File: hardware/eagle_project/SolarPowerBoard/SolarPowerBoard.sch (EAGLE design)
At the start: 82 parts, among them IC1 BQ29700DSET_BQ29700DSET, IC3 TPS63031DSKT_TPS63031DSKT, J2 105017-0001_105017-0001, J5 XG8S-0331_XG8S-0331, K1 G6E-134P-US_DC5_G6E-134P-US_D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, Q3 DAVIDE_FDN302P, U4 MCP73831T-2ACI_OT_MCP73831T-2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

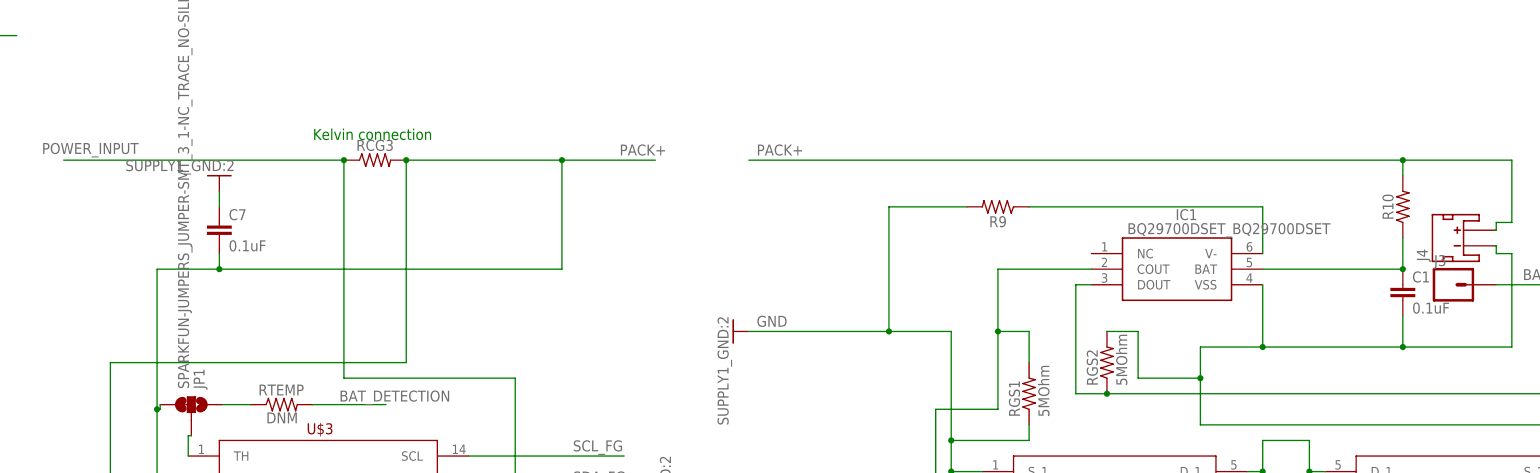
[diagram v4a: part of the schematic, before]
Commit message: Changed sense resistor
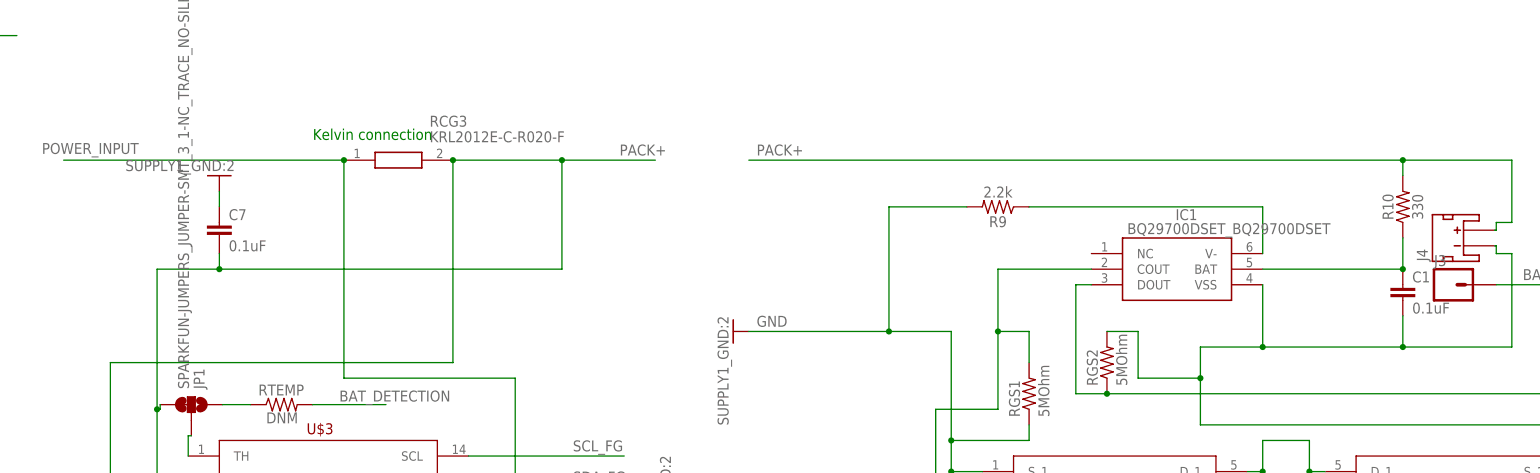
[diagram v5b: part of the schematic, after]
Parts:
- R10: value (none) -> 330
- R9: value (none) -> 2.2k
- RCG3: value (none) -> KRL2012E-C-R020-F; device SolarPowerBoard:SPARKFUN-RESISTORS_RESISTOR0805:1 -> SolarPowerBoard:KRL2012E-C-R020-F; OC_NEWARK unknown -> (none)
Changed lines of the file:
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@@
 <attribute name="OC_NEWARK" value="78X4150"/>
 </part>
-<part name="R9" library="SolarPowerBoard" deviceset="SPARKFUN-RESISTORS_RESISTOR*?:1" device="0805" value=" ">
+<part name="R9" library="SolarPowerBoard" deviceset="SPARKFUN-RESISTORS_RESISTOR*?:1" device="0805" value="2.2k">
 <attribute name="MF" value=""/>
 <attribute name="MPN" value="CR0805-FX-2201ELF"/>
 <attribute name="OC_NEWARK" value="06X5164"/>
 </part>
-<part name="R10" library="SolarPowerBoard" deviceset="SPARKFUN-RESISTORS_RESISTOR*?:1" device="0805" value=" ">
+<part name="R10" library="SolarPowerBoard" deviceset="SPARKFUN-RESISTORS_RESISTOR*?:1" device="0805" value="330">
 <attribute name="MF" value=""/>
 <attribute name="MPN" value="ERJ-6GEYJ331V"/>
@@
 </part>
 <part name="GND21" library="SolarPowerBoard" deviceset="SUPPLY1_GND*?:2" device=""/>
-<part name="RCG3" library="SolarPowerBoard" deviceset="SPARKFUN-RESISTORS_RESISTOR*?:1" device="0805" value=" ">
-<attribute name="MF" value=""/>
-<attribute name="MPN" value=""/>
-<attribute name="OC_NEWARK" value="unknown"/>
-</part>
 <part name="U$3" library="SolarPowerBoard" deviceset="SOLARCOMPONENTS_MAX17260" device="">
 <attribute name="MF" value=""/>
@@
 </part>
 <part name="L1" library="inductors" library_urn="urn:adsk.eagle:library:243" deviceset="EMC9714" device="" package3d_urn="urn:adsk.eagle:package:15060/1"/>
+<part name="RCG3" library="SolarPowerBoard" deviceset="KRL2012E-C-R020-F" device=""/>
 </parts>
 <sheets>
@@
 </instance>
 <instance part="GND21" gate="1" x="360.68" y="33.02" rot="R270"/>
-<instance part="RCG3" gate="G$1" x="302.26" y="60.96">
-<attribute name="NAME" x="302.26" y="62.484" size="1.778" layer="95" font="vector" align="bottom-center"/>
-<attribute name="VALUE" x="302.26" y="59.436" size="1.778" layer="96" font="vector" align="top-center"/>
-<attribute name="OC_NEWARK" x="302.26" y="60.96" size="1.778" layer="96" display="off"/>
-<attribute name="MF" x="302.26" y="60.96" size="1.778" layer="96" display="off"/>
-<attribute name="MPN" x="302.26" y="60.96" size="1.778" layer="96" display="off"/>
-</instance>
 <instance part="U$3" gate="G$1" x="294.64" y="5.08">
 <attribute name="NAME" x="291.084" y="16.256" size="1.778" layer="94"/>
@@
 <attribute name="NAME" x="24.13" y="75.946" size="1.778" layer="95"/>
 <attribute name="VALUE" x="24.003" y="70.612" size="1.778" layer="96"/>
+</instance>
+<instance part="RCG3" gate="G$1" x="297.18" y="60.96">
+<attribute name="NAME" x="311.15" y="67.31" size="1.778" layer="95" align="center-left"/>
+<attribute name="VALUE" x="311.15" y="64.77" size="1.778" layer="96" align="center-left"/>
 </instance>
 </instances>
@@
 <segment>
 <pinref part="U$3" gate="G$1" pin="CSN"/>
-<wire x1="307.34" y1="27.94" x2="259.08" y2="27.94" width="0.1524" layer="91"/>
+<wire x1="314.96" y1="27.94" x2="259.08" y2="27.94" width="0.1524" layer="91"/>
 <wire x1="259.08" y1="27.94" x2="259.08" y2="-17.78" width="0.1524" layer="91"/>
 <wire x1="259.08" y1="-17.78" x2="271.78" y2="-17.78" width="0.1524" layer="91"/>
@@
 <wire x1="266.7" y1="20.32" x2="266.7" y2="43.18" width="0.1524" layer="91"/>
 <wire x1="266.7" y1="43.18" x2="276.86" y2="43.18" width="0.1524" layer="91"/>
-<pinref part="RCG3" gate="G$1" pin="2"/>
 <wire x1="276.86" y1="43.18" x2="332.74" y2="43.18" width="0.1524" layer="91"/>
-<wire x1="332.74" y1="60.96" x2="307.34" y2="60.96" width="0.1524" layer="91"/>
+<wire x1="332.74" y1="60.96" x2="314.96" y2="60.96" width="0.1524" layer="91"/>
 <wire x1="332.74" y1="43.18" x2="332.74" y2="60.96" width="0.1524" layer="91"/>
 <wire x1="276.86" y1="43.18" x2="276.86" y2="45.72" width="0.1524" layer="91"/>
 <junction x="276.86" y="43.18"/>
 <pinref part="C7" gate="G$1" pin="2"/>
-<wire x1="307.34" y1="27.94" x2="307.34" y2="60.96" width="0.1524" layer="91"/>
-<junction x="307.34" y="60.96"/>
+<wire x1="314.96" y1="27.94" x2="314.96" y2="60.96" width="0.1524" layer="91"/>
 <pinref part="JP1" gate="G$1" pin="3"/>
 <wire x1="267.208" y1="21.082" x2="267.208" y2="20.32" width="0.1524" layer="91"/>
@@
 <junction x="332.74" y="60.96"/>
 <label x="342.138" y="61.722" size="1.778" layer="95"/>
+<pinref part="RCG3" gate="G$1" pin="2"/>
+<junction x="314.96" y="60.96"/>
 </segment>
 </net>
@@
 <pinref part="U$3" gate="G$1" pin="CSPH"/>
 <wire x1="317.5" y1="-7.62" x2="325.12" y2="-7.62" width="0.1524" layer="91"/>
-<pinref part="RCG3" gate="G$1" pin="1"/>
 <wire x1="297.18" y1="25.4" x2="297.18" y2="60.96" width="0.1524" layer="91"/>
 <wire x1="251.46" y1="60.96" x2="297.18" y2="60.96" width="0.1524" layer="91"/>
+<label x="247.904" y="61.976" size="1.778" layer="95"/>
+<pinref part="RCG3" gate="G$1" pin="1"/>
 <junction x="297.18" y="60.96"/>
-<label x="247.904" y="61.976" size="1.778" layer="95"/>
-</segment>
-<segment>
+</segment>
+<segment>

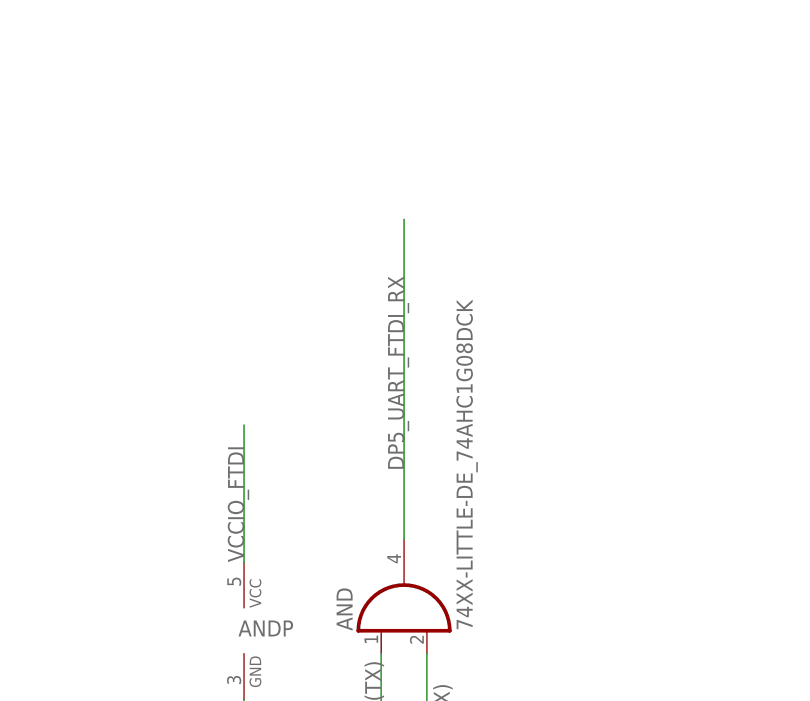
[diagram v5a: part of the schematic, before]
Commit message: Added 0ohm resistor between UART AND port and RX pin. Removed library autosave files.
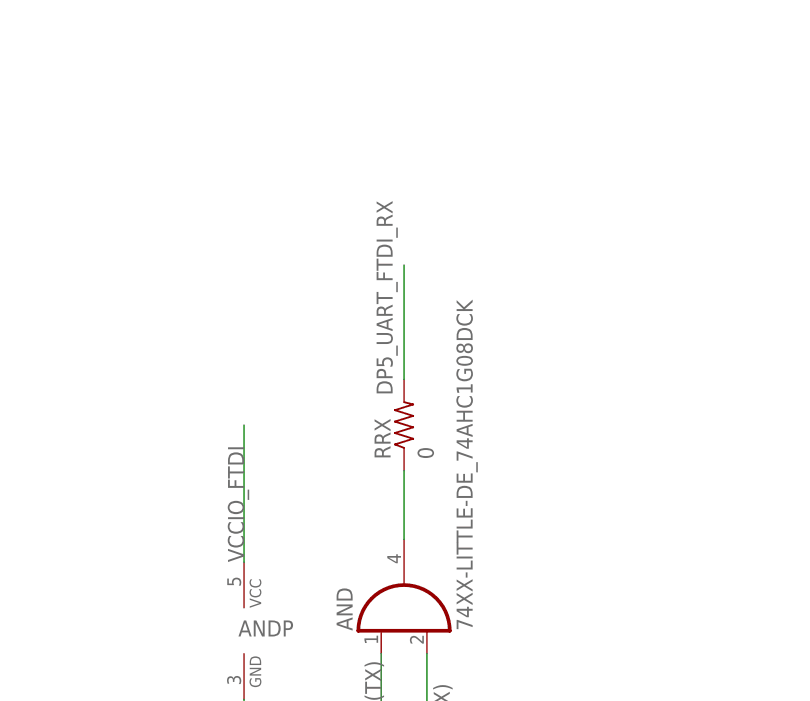
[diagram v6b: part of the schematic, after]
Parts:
- added RRX: 0, resistor:R-US_R0805
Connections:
- net DP5_UART_FTDI_RX: now also RRX.1, RRX.2
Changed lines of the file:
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@@
 <part name="L1" library="inductors" library_urn="urn:adsk.eagle:library:243" deviceset="EMC9714" device="" package3d_urn="urn:adsk.eagle:package:15060/1"/>
 <part name="RCG3" library="SolarPowerBoard" deviceset="KRL2012E-C-R020-F" device=""/>
+<part name="RRX" library="resistor" library_urn="urn:adsk.eagle:library:348" deviceset="R-US_" device="R0805" package3d_urn="urn:adsk.eagle:package:23553/2" value="0"/>
 </parts>
 <sheets>
@@
 <attribute name="NAME" x="311.15" y="67.31" size="1.778" layer="95" align="center-left"/>
 <attribute name="VALUE" x="311.15" y="64.77" size="1.778" layer="96" align="center-left"/>
+</instance>
+<instance part="RRX" gate="G$1" x="-83.82" y="104.14" rot="R90">
+<attribute name="NAME" x="-85.3186" y="100.33" size="1.778" layer="95" rot="R90"/>
+<attribute name="VALUE" x="-80.518" y="100.33" size="1.778" layer="96" rot="R90"/>
 </instance>
 </instances>
@@
 <net name="DP5_UART_FTDI_RX" class="0">
 <segment>
-<pinref part="AND" gate="A" pin="O"/>
-<wire x1="-83.82" y1="91.44" x2="-83.82" y2="127" width="0.1524" layer="91"/>
-<label x="-83.82" y="99.06" size="1.778" layer="95" rot="R90"/>
-</segment>
-<segment>
 <pinref part="FT230XQ-R" gate="G$1" pin="RXD"/>
 <pinref part="RX_TX" gate="G$1" pin="2"/>
@@
 <label x="102.616" y="156.718" size="1.778" layer="95"/>
 </segment>
+<segment>
+<pinref part="AND" gate="A" pin="O"/>
+<wire x1="-83.82" y1="91.44" x2="-83.82" y2="99.06" width="0.1524" layer="91"/>
+<pinref part="RRX" gate="G$1" pin="1"/>
+</segment>
+<segment>
+<pinref part="RRX" gate="G$1" pin="2"/>
+<wire x1="-83.82" y1="109.22" x2="-83.82" y2="121.92" width="0.1524" layer="91"/>
+<label x="-85.09" y="107.442" size="1.778" layer="95" rot="R90"/>
+</segment>
 </net>

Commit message: commiting the PCB printed ad eurocircuit (very first version)
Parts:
- removed C1-1, C1-2: 4.7uF, SolarPowerBoard:SPARKFUN-CAPACITORS_4.7UF0603
- removed D5: RED, SolarPowerBoard:SPARKFUN-LED_LED0603
- removed IC1: BQ29700DSET_BQ29700DSET, SolarPowerBoard:BQ29700DSET_BQ29700DSET
- removed RCG3: KRL2012E-C-R020-F, SolarPowerBoard:KRL2012E-C-R020-F
- removed RX: ORANGE, SparkFun-LED:LED0603
- removed TX: YELLOW, SparkFun-LED:LED0603
- added C13: 10u, SolarPowerBoard:SPARKFUN-CAPACITORS_10UF-0805-10V-10%
- added LED_CH, LED_RX, LED_TX: (no value), SolarPowerBoard:LED0603
- added R5: 0.02, SolarPowerBoard:FCSL90R020DER
- added U6: MCP73831T-2ACI_OT_MCP73831T-2ACI/OT, SolarPowerBoard:MCP73831T-2ACI_OT_MCP73831T-2ACI/OT
- C1, C7, CMPP: value 0.1uF -> 100n; device SolarPowerBoard:SPARKFUN-CAPACITORS_0.1UF-0603-100V-10% -> SolarPowerBoard:SPARKFUN-CAPACITORS_10UF-0805-10V-10%; MF (none) -> AVX CORPORATION; MPN MC0603B104K160CT -> TPSP106M010R2000; OC_NEWARK 06R4923 -> 22K2788
- C10: value 470nF -> 470n; device SolarPowerBoard:RESISTOR_C-EUC0805 -> SolarPowerBoard:SPARKFUN-CAPACITORS_10UF-0805-10V-10%; MF (none) -> AVX CORPORATION; MPN C0805C474K8RACTU -> TPSP106M010R2000; OC_NEWARK 07X0956 -> 22K2788
- C11, C12: device SolarPowerBoard:SPARKFUN-CAPACITORS_CAP0603-CAP -> SolarPowerBoard:SPARKFUN-CAPACITORS_10UF-0805-10V-10%; MF (none) -> AVX CORPORATION; MPN (none) -> TPSP106M010R2000; OC_NEWARK (none) -> 22K2788
- C14: value 10nF -> 10n
- C15, C16: value 47pF -> 47p
- C2, C3, C4: value 10uF -> 10u
- C24, C26, C8, C9: value 100nF -> 100n
- C25: value 4.7uF -> 4.7u
- C5: value 0.1uF -> 100n; device SolarPowerBoard:SPARKFUN-CAPACITORS_0.1UF-0603-25V-5% -> SolarPowerBoard:SPARKFUN-CAPACITORS_10UF-0805-10V-10%; MF (none) -> AVX CORPORATION; MPN MC0603B104K160CT -> TPSP106M010R2000; OC_NEWARK 06R4923 -> 22K2788
- C6: value 470pF -> 470p; device SolarPowerBoard:SPARKFUN-CAPACITORS_470PF-0603-50V-5% -> SolarPowerBoard:SPARKFUN-CAPACITORS_10UF-0805-10V-10%; MF KEMET -> AVX CORPORATION; MPN C0603C471K4RACTU -> TPSP106M010R2000; OC_NEWARK 03H3923 -> 22K2788
- CF: value 1.0uF -> 1.0u
- COUT1: value 10uF -> 10u; device SolarPowerBoard:RESISTOR_C-EUC0805 -> SolarPowerBoard:SPARKFUN-CAPACITORS_10UF-0805-10V-10%; MF (none) -> AVX CORPORATION; MPN C2012X7R1A106M125AC -> TPSP106M010R2000; OC_NEWARK 04X3283 -> 22K2788
- COUT2: value 33uF -> 33u; device SolarPowerBoard:RESISTOR_C-EUC0805 -> SolarPowerBoard:SPARKFUN-CAPACITORS_10UF-0805-10V-10%; MF (none) -> AVX CORPORATION; MPN TLJP336M010R3500 -> TPSP106M010R2000; OC_NEWARK 64M1270 -> 22K2788
- J3: value (none) -> BAT_ID
- L1: value EMC9714 -> 27u; device inductors:EMC9714 -> SolarPowerBoard:INDUCTOR_TH; MPN (none) -> B82144F2273K000
- L2: value SRN3010-470M_SRN3010-470M -> 47u
- L3: value MI0805K601R-10 -> DAVIDE_FERRITE_BREAD; MPN (none) -> MI0805K601R-10
- R1: device SolarPowerBoard:RESISTOR_R-US_R0805 -> SolarPowerBoard:SPARKFUN-RESISTORS_0.3OHM-0805-1/8W-1%; MPN ERA-6AEB105V -> RLP73N2AR30JTD; OC_NEWARK 08N2144 -> 43AC3996
- R2: device SolarPowerBoard:RESISTOR_R-US_R0805 -> SolarPowerBoard:SPARKFUN-RESISTORS_0.3OHM-0805-1/8W-1%; MPN ERJ-6GEYJ274V -> RLP73N2AR30JTD; OC_NEWARK 53W4949 -> 43AC3996
- R27, R28: value 470 -> 680; device SparkFun-Resistors:0.3OHM-0805-1/8W-1% -> SolarPowerBoard:SPARKFUN-RESISTORS_0.3OHM-0805-1/8W-1%; MPN (none) -> RLP73N2AR30JTD; OC_NEWARK (none) -> 43AC3996
- R3, RF1, RF2: device SolarPowerBoard:RESISTOR_R-US_R0805 -> SolarPowerBoard:SPARKFUN-RESISTORS_0.3OHM-0805-1/8W-1%; MPN ERJ-6ENF1001V -> RLP73N2AR30JTD; OC_NEWARK 64R5369 -> 43AC3996
- R8: device SolarPowerBoard:RESISTOR_R-US_R0805 -> SolarPowerBoard:SPARKFUN-RESISTORS_0.3OHM-0805-1/8W-1%; MPN MC0805S8F0000T5E -> RLP73N2AR30JTD; OC_NEWARK 79M6013 -> 43AC3996
- RGPIO1, RGPIO2, RGPIO3, RGPIO4: value (none) -> 1k; device SolarPowerBoard:SPARKFUN-RESISTORS_RESISTOR0603:1 -> SolarPowerBoard:SPARKFUN-RESISTORS_0.3OHM-0805-1/8W-1%; MPN (none) -> RLP73N2AR30JTD; OC_NEWARK (none) -> 43AC3996
- RGS1, RGS2: value 5MOhm -> 5M; device SolarPowerBoard:RESISTOR_R-US_R0805 -> SolarPowerBoard:SPARKFUN-RESISTORS_RESISTOR0805:1; MPN HVC0805T5004JET -> ERJ-6GEYJ331V; OC_NEWARK 55X2811 -> 65T8817
- RLED1, RPROG1: device SolarPowerBoard:SPARKFUN-PASSIVES_RESISTOR0603-RES -> SolarPowerBoard:SPARKFUN-RESISTORS_0.3OHM-0805-1/8W-1%; MPN (none) -> RLP73N2AR30JTD; OC_NEWARK (none) -> 43AC3996
- RRX: value 0 -> 1k; device resistor:R-US_R0805 -> SolarPowerBoard:SPARKFUN-RESISTORS_0.3OHM-0805-1/8W-1%; MPN (none) -> RLP73N2AR30JTD; OC_NEWARK (none) -> 43AC3996
- RS1: value RL1220T-R010-J_RL1220T-R010-J -> 0.01
- RTEMP: device SolarPowerBoard:RESISTOR_R-US_R0805 -> SolarPowerBoard:SPARKFUN-RESISTORS_RESISTOR0805:1; MPN (none) -> ERJ-6GEYJ331V; OC_NEWARK (none) -> 65T8817
- U3: value FT230XQ-R -> FT230XQ_FT230XQ_2
- U4: value MCP73831T-2ACI_OT_MCP73831T-2ACI/OT -> BQ29700DSET_BQ29700DSET; device SolarPowerBoard:MCP73831T-2ACI_OT_MCP73831T-2ACI/OT -> SolarPowerBoard:BQ29700DSET_BQ29700DSET; MPN (none) -> BQ29700DSET; OC_NEWARK (none) -> 78X4150
- renumbered AND to U7, CHG2 to Q1, DCH2 to Q2, FT230XQ-R to U3, IC3 to U5, RB2 to B1, U$1 to U1, U$2 to B2, U$3 to U2
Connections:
- net DP4_UART_FTDI_TX renamed FTDI_TX
- removed net N$23: K1.GND
- new net FTDI_RX: RRX.2, RX_TX.2, U3.RXD
- net BAT_DETECTION: now also RTEMP.1; no longer RTEMP.2
- net DP5_UART_FTDI_RX: no longer RRX.2, RX_TX.2, U3.RXD
- net GND: now also C10.1, C13.2, COUT1.2, COUT2.2, K1.GND, U6.VSS; no longer C1-1.2, C1-2.2, C10.2, COUT1.1, COUT2.1, U4.VSS
- net GPIO1: now also RGPIO1.1; no longer RGPIO1.2
- net GPIO2: now also RGPIO2.1; no longer RGPIO2.2
- net GPIO3: now also RGPIO3.1; no longer RGPIO3.2
- net GPIO4: now also RGPIO4.1; no longer RGPIO4.2
- net N$1: now also C13.1, R3.2; no longer C1-1.1, C1-2.1, R3.1
- net N$13: now also RLED1.2, U6.STAT; no longer RLED1.1, U4.STAT
- net N$15: now also U4.COUT; no longer IC1.COUT
- net N$19: now also U4.VSS; no longer IC1.VSS
- net N$2: now also U6.PROG; no longer U4.PROG
- net N$20: now also C11.1, U6.VBAT; no longer C12.1, U4.VBAT
- net N$21: now also RTEMP.2; no longer RTEMP.1
- net N$22: now also U4.DOUT; no longer IC1.DOUT
- net N$24: now also U4.BAT; no longer IC1.BAT
- net N$28: now also RGPIO1.2; no longer RGPIO1.1
- net N$29: now also U4.V-; no longer IC1.V-
- net N$3: now also R3.1, R8.2; no longer R3.2, R8.1
- net N$30: now also RGPIO2.2; no longer RGPIO2.1
- net N$31: now also R28.2; no longer R28.1
- net N$32: now also LED_RX.C, R28.1; no longer R28.2, RX.C
- net N$33: now also RGPIO3.2; no longer RGPIO3.1
- net N$4: now also R8.1; no longer R8.2
- net N$41: now also RGPIO4.2; no longer RGPIO4.1
- net N$42: now also LED_TX.C, R27.1; no longer R27.2, TX.C
- net N$43: now also R27.2; no longer R27.1
- net N$45: now also C10.2; no longer C10.1
- net N$5: now also COUT1.1, RF1.1; no longer COUT1.2, RF1.2
- net N$6: now also RF1.2; no longer RF1.1
- net N$7: now also RF2.2; no longer RF2.1
- net N$9: now also LED_CH.C, RLED1.1; no longer D5.C, RLED1.2
- net PACK+: now also R5.2; no longer RCG3.2
- net POWER_INPUT: now also R5.1; no longer RCG3.1
- net SOLAR_OUTPUT: now also COUT2.1, RF2.1; no longer COUT2.2, RF2.2
- net VCCIO_FTDI: now also LED_RX.A, LED_TX.A; no longer RX.A, TX.A
- net VDD_CHARGER: now also C12.1, LED_CH.A, U6.VDD; no longer C11.1, D5.A, U4.VDD
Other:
- moved on the sheet: C10, C11, C12, COUT1, COUT2, R27, R28, R3, R8, RF1, RF2, RGPIO1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

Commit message: PCB project update
- arduino header fix
- text fix
- library refactor (now all the capacitor use the same component as well as resistors)
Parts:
- added C17: 4.7u, SolarPowerBoard:SPARKFUN-CAPACITORS_10UF-0805-10V-10%
- C13: value 10u -> 4.7u
- C14, C15, C16, C24, C25, C26, C8, C9: device SolarPowerBoard:SPARKFUN-CAPACITORS_10UF-0805-10V-10%:1 -> SolarPowerBoard:SPARKFUN-CAPACITORS_10UF-0805-10V-10%
- CF: value 1.0u -> 1u; device SolarPowerBoard:SPARKFUN-CAPACITORS_1.0UF-0805-25V-(+80/-20%) -> SolarPowerBoard:SPARKFUN-CAPACITORS_10UF-0805-10V-10%; MF (none) -> AVX CORPORATION; MPN C0805C105J4RACTU -> TPSP106M010R2000; OC_NEWARK 07X0871 -> 22K2788
- R1, R14, R15, R2, R23, R24, R25, R26, R27, R28, R29, R3, R4, R8, RF1, RF2, RGPIO1, RGPIO2, RGPIO3, RGPIO4, RPROG1, RRX: device SolarPowerBoard:SPARKFUN-RESISTORS_0.3OHM-0805-1/8W-1% -> SolarPowerBoard:SPARKFUN-RESISTORS_0.3OHM
- R10, RGS1, RGS2, RTEMP: device SolarPowerBoard:SPARKFUN-RESISTORS_RESISTOR0805:1 -> SolarPowerBoard:SPARKFUN-RESISTORS_0.3OHM; MPN ERJ-6GEYJ331V -> RLP73N2AR30JTD; OC_NEWARK 65T8817 -> 43AC3996
- R9: device SolarPowerBoard:SPARKFUN-RESISTORS_RESISTOR0805:1 -> SolarPowerBoard:SPARKFUN-RESISTORS_0.3OHM; MPN CR0805-FX-2201ELF -> RLP73N2AR30JTD; OC_NEWARK 06X5164 -> 43AC3996
- RLED1: value 680 -> 1k; device SolarPowerBoard:SPARKFUN-RESISTORS_0.3OHM-0805-1/8W-1% -> SolarPowerBoard:SPARKFUN-RESISTORS_0.3OHM
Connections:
- net BAT_DETECTION: now also RTEMP.2; no longer RTEMP.1
- net GND: now also C17.2, RGS1.2; no longer RGS1.1
- net N$1: now also C17.1
- net N$15: now also RGS1.1; no longer RGS1.2
- net N$19: now also RGS2.1; no longer RGS2.2
- net N$21: now also RTEMP.1; no longer RTEMP.2
- net N$22: now also RGS2.2; no longer RGS2.1
- net N$24: now also R10.2; no longer R10.1
- net PACK+: now also R10.1; no longer R10.2
- net VCCIO_FTDI: now also C26.1; no longer C24.1
- net VCC_FTDI: now also C24.1; no longer C26.1
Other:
- moved on the sheet: C14, C24, C26, R10, RGS1, RGS2, RTEMP
